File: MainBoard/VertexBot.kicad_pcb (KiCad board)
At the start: 2 copper layers, 115.6 x 107.8 mm, 47 parts, among them J1 Battery, J4 Left Motor, J5 Right Motor, J6 Led Strip, Q1 BSS138, Q2 BSS138, Q3 BSS138, SW1 SW_SPST, U1 DRV8830DGQR, U10 MAX4466, U11 MAX4466, U12 ESP32-S3-CAM-B, U13 ESP32-S3-CAM-A, U14 MAX98357A, U2 DRV8830DGQR, U3 S13V30F5, U5 INMP441, U6 0.96 INCH OLED, U7 DRV5033AJxLPG, U8 DRV5033AJxLPG, U9 MPU 6050

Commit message: Fix for correct battery connector footprint
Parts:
- J1: footprint Connector_JST:JST_XH_S3B-XH-A-1_1x03_P2.50mm_Horizontal -> Connector_JST:JST_XH_S2B-XH-A-1_1x02_P2.50mm_Horizontal
- moved J1 49.0 mm to (158.0, 113.6), turned to -125.5 degrees
- moved U5 16.5 mm to (107.3, 129.7)
- moved U9 4.93 mm to (147.2, 88.8)

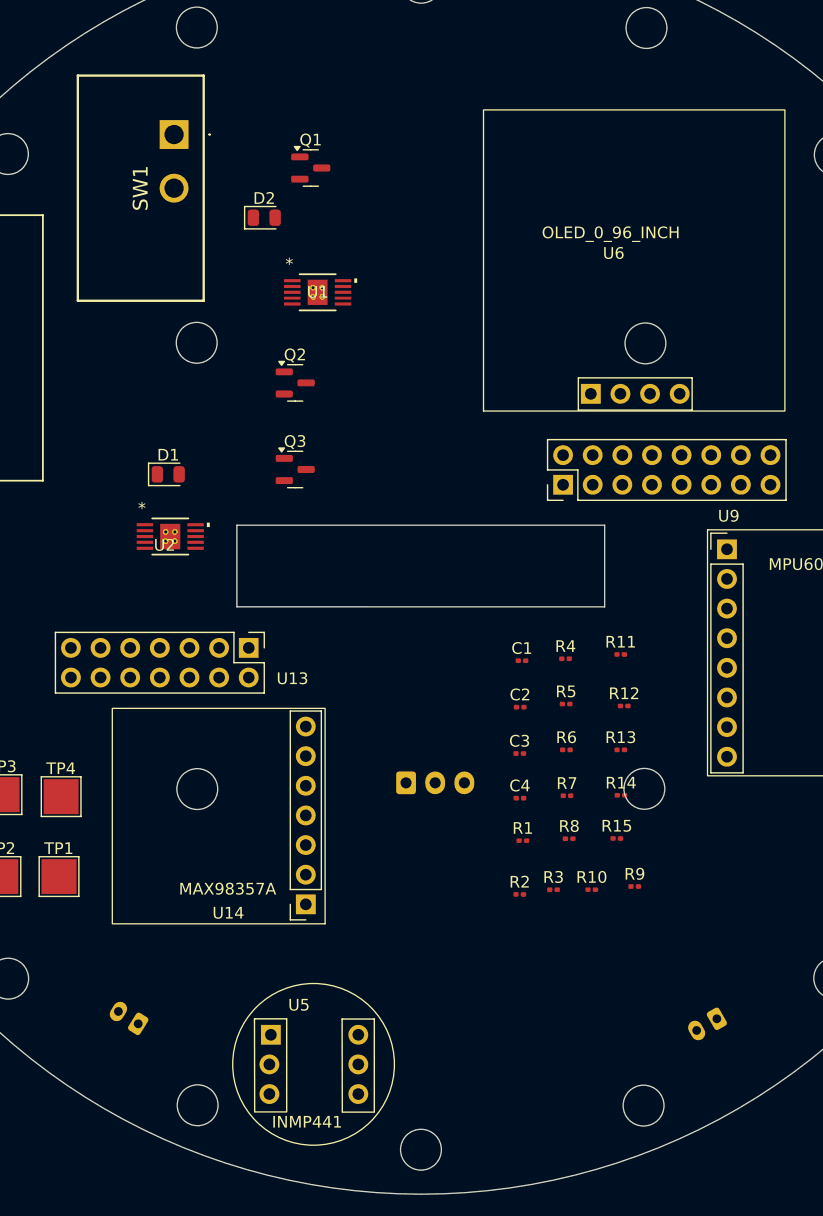
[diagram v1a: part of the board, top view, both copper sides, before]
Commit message: Adjust divider values for cutoff at 3V (en = 1V) Add Tolerance (0.1%)
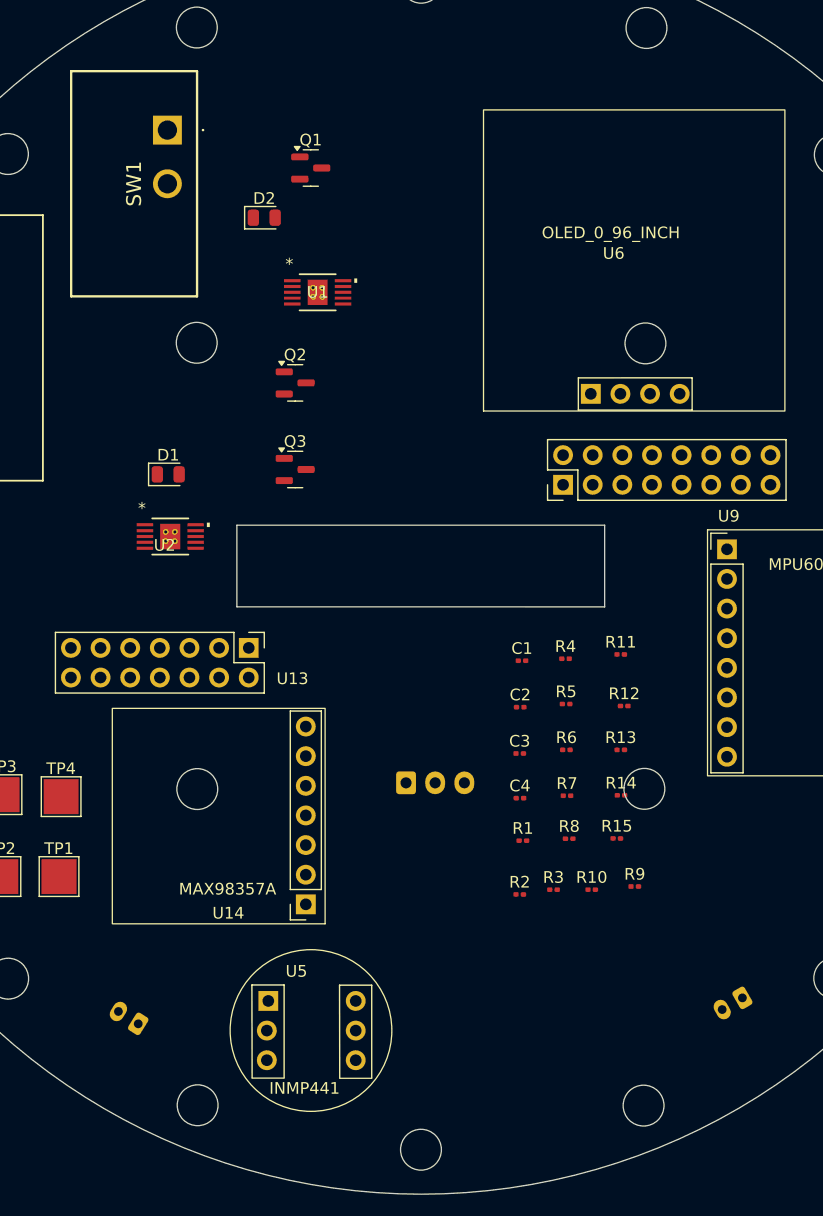
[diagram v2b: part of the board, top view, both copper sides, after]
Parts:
- moved U5 2.91 mm to (107.0, 126.8)
- moved J4 2.83 mm to (147.8, 126.5)
- moved SW1 0.69 mm to (98.5, 52.1)
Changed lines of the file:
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@@
 	(footprint "Vertex_Bot:L101011MS02Q"
 		(layer "F.Cu")
-		(at 99.09 52.52 -90)
+		(at 98.52 52.14 -90)
 		(descr "L101011MS02Q-2")
 		(tags "Switch")
@@
 	(footprint "Vertex_Bot:INMP441"
 		(layer "F.Cu")
-		(at 107.26 129.68)
+		(at 107.04 126.78)
 		(property "Reference" "U5"
 			(at 2.54 -2.54 0)
@@
 	(footprint "Connector_JST:JST_PH_S2B-PH-K_1x02_P2.00mm_Horizontal"
 		(layer "B.Cu")
-		(at 145.612051 128.31 -150)
+		(at 147.801026 126.518238 -150)
 		(descr "JST PH series connector, S2B-PH-K (http://www.jst-mfg.com/product/pdf/eng/ePH.pdf), generated with kicad-footprint-generator")
 		(tags "connector JST PH horizontal")
 		(property "Reference" "J4"
-			(at 1 2.55 30)
+			(at 0.999999 2.550002 30)
 			(layer "B.SilkS")
 			(effects
@@
 		)
 		(property "Value" "Left Motor"
-			(at 1 -7.45 30)
+			(at 1.000001 -7.449998 30)
 			(layer "B.Fab")
 			(effects
@@
 		(fp_line
 			(start 3.14 1.46)
-			(end 3.14 -0.14)
+			(end 3.14 -0.140002)
 			(stroke
 				(width 0.12)
@@
 		(fp_line
 			(start 4.06 -0.14)
-			(end 3.14 -0.14)
+			(end 3.14 -0.140002)
 			(stroke
 				(width 0.12)
@@
 		)
 		(fp_line
-			(start 3.14 -0.14)
+			(start 3.14 -0.140002)
 			(end 2.860001 -0.14)
 			(stroke
@@
 		(fp_line
 			(start 3.3 -2.5)
-			(end 3.3 -4.1)
+			(end 3.3 -4.100001)
 			(stroke
 				(width 0.12)
@@
 		)
 		(fp_line
-			(start 3.3 -4.1)
+			(start 3.3 -4.100001)
 			(end 2.3 -4.1)
 			(stroke
@@
 		)
 		(fp_line
-			(start 2.3 -2.500001)
+			(start 2.3 -2.500002)
 			(end 3.3 -2.5)
 			(stroke
@@
 		(fp_line
 			(start 2.3 -4.1)
-			(end 2.3 -2.500001)
+			(end 2.3 -2.500002)
 			(stroke
 				(width 0.12)
@@
 		(fp_line
 			(start -1.14 1.46)
-			(end -2.06 1.46)
+			(end -2.059999 1.460001)
 			(stroke
 				(width 0.12)
@@
 		)
 		(fp_line
-			(start -0.86 -0.14)
-			(end -0.86 1.075)
+			(start -0.860001 -0.140001)
+			(end -0.86 1.075001)
 			(stroke
 				(width 0.12)
@@
 		)
 		(fp_line
-			(start -0.86 -0.14)
+			(start -0.860001 -0.140001)
 			(end -1.14 -0.14)
 			(stroke
@@
 		)
 		(fp_line
-			(start -2.06 1.46)
-			(end -2.059999 -6.36)
+			(start -2.059999 1.460001)
+			(end -2.060002 -6.36)
 			(stroke
 				(width 0.12)
@@
 		(fp_line
 			(start -0.3 -2.500001)
-			(end -1.3 -2.5)
+			(end -1.299999 -2.5)
 			(stroke
 				(width 0.12)
@@
 		)
 		(fp_line
-			(start -2.059999 -0.14)
+			(start -2.06 -0.140001)
 			(end -1.14 -0.14)
 			(stroke
@@
 		)
 		(fp_line
-			(start -0.3 -4.1)
+			(start -0.299999 -4.1)
 			(end -0.3 -2.500001)
 			(stroke
@@
 		)
 		(fp_line
-			(start -0.3 -4.1)
-			(end -0.3 -6.360001)
+			(start -0.299999 -4.1)
+			(end -0.299998 -6.36)
 			(stroke
 				(width 0.12)
@@
 		)
 		(fp_line
-			(start -1.3 -2.5)
-			(end -1.3 -4.1)
+			(start -1.299999 -2.5)
+			(end -1.300001 -4.099999)
 			(stroke
 				(width 0.12)
@@
 		(fp_line
 			(start -0.8 -4.1)
-			(end -0.8 -6.36)
+			(end -0.799998 -6.360001)
 			(stroke
 				(width 0.12)
@@
 		)
 		(fp_line
-			(start 0.5 -6.36)
+			(start 0.500001 -6.36)
 			(end 0.5 -2)
 			(stroke
@@
 		)
 		(fp_line
-			(start -1.3 -4.1)
-			(end -0.3 -4.1)
+			(start -1.300001 -4.099999)
+			(end -0.299999 -4.1)
 			(stroke
 				(width 0.12)
@@
 		)
 		(fp_line
-			(start -2.059999 -6.36)
+			(start -2.060002 -6.36)
 			(end 4.06 -6.36)
 			(stroke
@@
 		(fp_line
 			(start -2.45 1.85)
-			(end -2.45 -6.749999)
+			(end -2.449999 -6.749999)
 			(stroke
 				(width 0.05)
@@
 		)
 		(fp_line
-			(start -2.45 -6.749999)
+			(start -2.449999 -6.749999)
 			(end 4.45 -6.75)
 			(stroke
@@
 		)
 		(fp_line
-			(start 3.95 1.35)
+			(start 3.949999 1.349998)
 			(end 3.250001 1.35)
 			(stroke
@@
 		)
 		(fp_line
-			(start 3.95 -6.25)
-			(end 3.95 1.35)
+			(start 3.95 -6.250003)
+			(end 3.949999 1.349998)
 			(stroke
 				(width 0.1)
@@
 		(fp_line
 			(start -1.25 1.35)
-			(end -1.95 1.35)
+			(end -1.95 1.350001)
 			(stroke
 				(width 0.1)
@@
 		)
 		(fp_line
-			(start -1.95 1.35)
-			(end -1.95 -6.25)
+			(start -1.95 1.350001)
+			(end -1.950001 -6.25)
 			(stroke
 				(width 0.1)
@@
 		)
 		(fp_line
-			(start -1.95 -6.25)
-			(end 3.95 -6.25)
+			(start -1.950001 -6.25)
+			(end 3.95 -6.250003)
 			(stroke
 				(width 0.1)

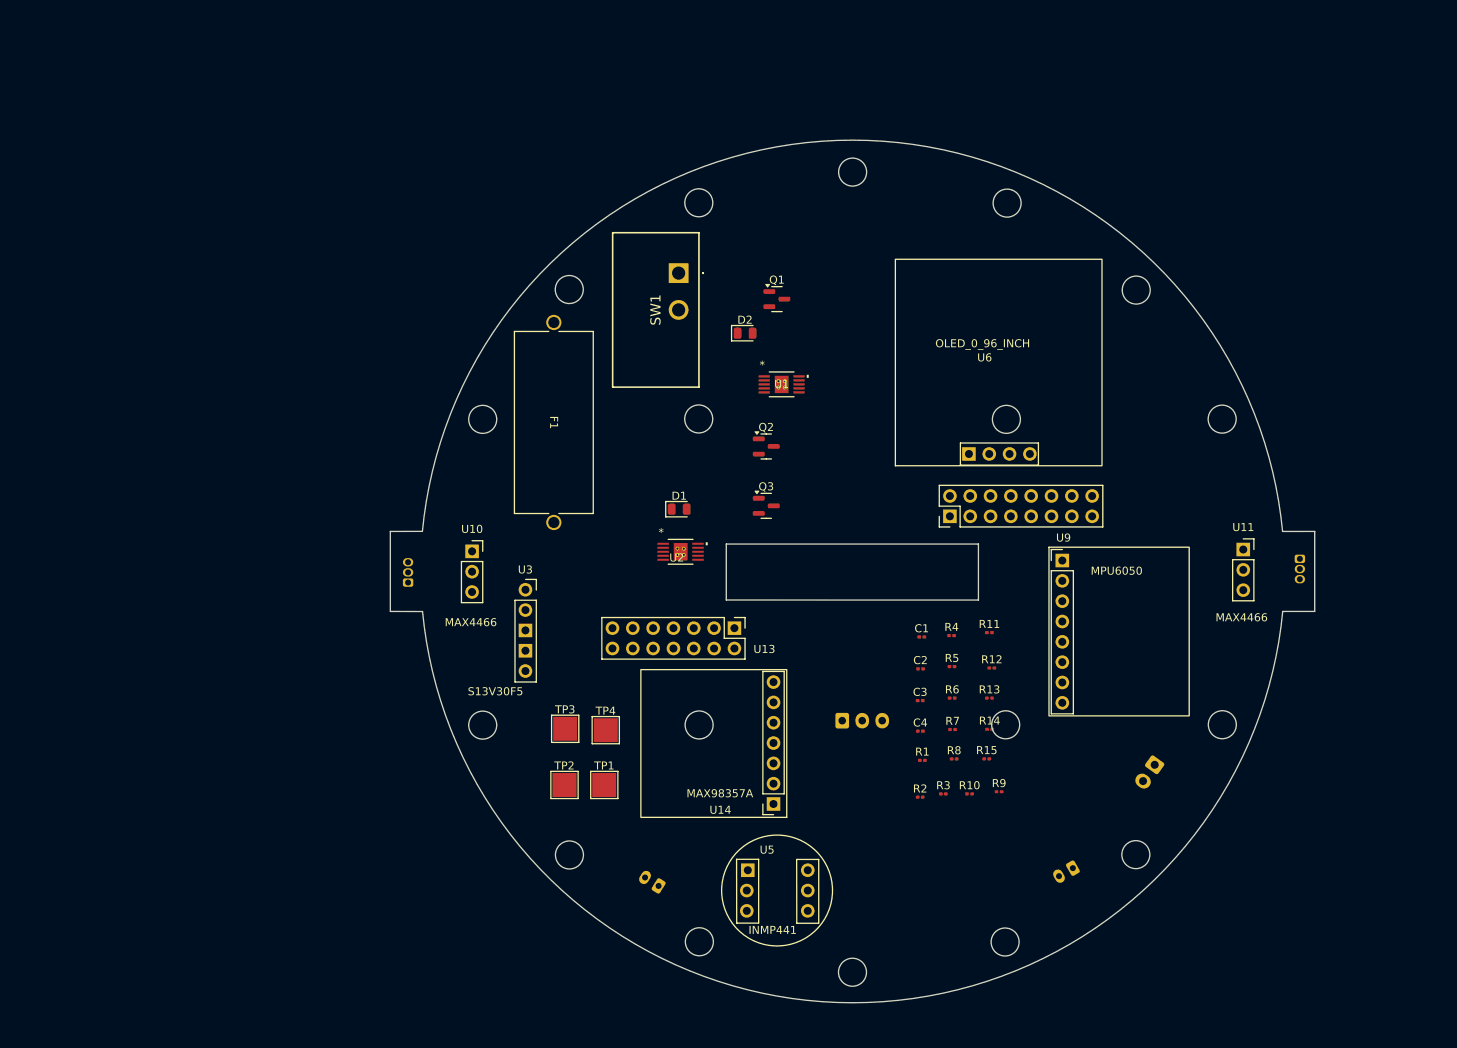
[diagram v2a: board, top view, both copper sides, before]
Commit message: - Relayed schematic with better modular approach (Global labels usage) - Edge cut so that now backboards are facing to the sides, central rectangular hole rotated by 90 - Some fooprints DRC'ed and fixed (more to come)
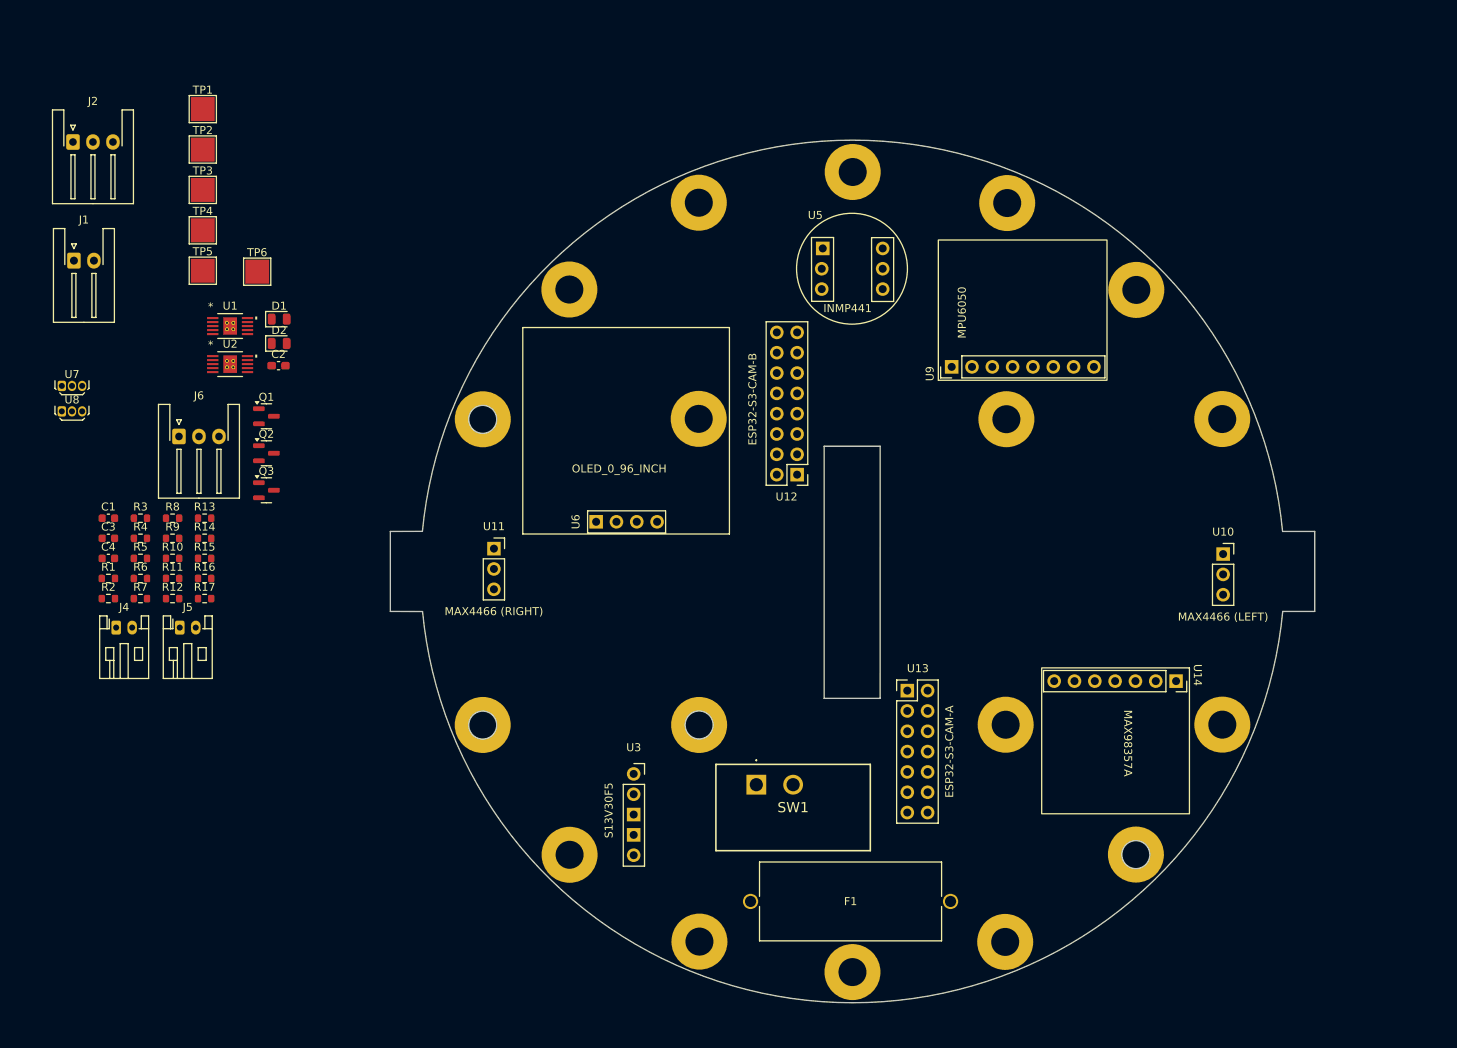
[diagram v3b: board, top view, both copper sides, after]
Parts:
- added H1: MountingHole, MountingHole:MountingHole_3.5mm_Pad, F.Cu at (139.5, 70.4)
- added H10: MountingHole, MountingHole:MountingHole_3.5mm_Pad, F.Cu at (155.7, 124.8)
- added H11: MountingHole, MountingHole:MountingHole_3.5mm_Pad, F.Cu at (139.3, 135.7)
- added H12: MountingHole, MountingHole:MountingHole_3.5mm_Pad, F.Cu at (120.2, 139.5)
- added H13: MountingHole, MountingHole:MountingHole_3.5mm_Pad, F.Cu at (101.1, 135.7)
- added H14: MountingHole, MountingHole:MountingHole_3.5mm_Pad, F.Cu at (84.9, 124.8)
- added H15: MountingHole, MountingHole:MountingHole_3.5mm_Pad, F.Cu at (74.0, 108.6)
- added H16: MountingHole, MountingHole:MountingHole_3.5mm_Pad, F.Cu at (74.0, 70.4)
- added H17: MountingHole, MountingHole:MountingHole_3.5mm_Pad, F.Cu at (84.9, 54.2)
- added H18: MountingHole, MountingHole:MountingHole_3.5mm_Pad, F.Cu at (101.0, 43.3)
- added H2: MountingHole, MountingHole:MountingHole_3.5mm_Pad, F.Cu at (101.0, 70.4)
- added H3: MountingHole, MountingHole:MountingHole_3.5mm_Pad, F.Cu at (101.1, 108.6)
- added H4: MountingHole, MountingHole:MountingHole_3.5mm_Pad, F.Cu at (139.4, 108.6)
- added H5: MountingHole, MountingHole:MountingHole_3.5mm_Pad, F.Cu at (120.3, 39.5)
- added H6: MountingHole, MountingHole:MountingHole_3.5mm_Pad, F.Cu at (139.6, 43.4)
- added H7: MountingHole, MountingHole:MountingHole_3.5mm_Pad, F.Cu at (155.7, 54.2)
- added H8: MountingHole, MountingHole:MountingHole_3.5mm_Pad, F.Cu at (166.5, 70.4)
- added H9: MountingHole, MountingHole:MountingHole_3.5mm_Pad, F.Cu at (166.5, 108.6)
- added J2: I2C Extension, Connector_JST:JST_XH_S3B-XH-A-1_1x03_P2.50mm_Horizontal, F.Cu at (22.8, 35.8)
- added R16: 0.44, Resistor_SMD:R_0603_1608Metric, F.Cu at (39.3, 90.3)
- added R17: 0.44, Resistor_SMD:R_0603_1608Metric, F.Cu at (39.3, 92.8)
- added TP5: TestPoint_Flag, TestPoint:TestPoint_Pad_3.0x3.0mm, F.Cu at (39.0, 51.8)
- added TP6: TestPoint_Flag, TestPoint:TestPoint_Pad_3.0x3.0mm, F.Cu at (45.8, 52.0)
- C1: footprint Capacitor_SMD:C_0201_0603Metric -> Capacitor_SMD:C_0603_1608Metric
- C2: footprint Capacitor_SMD:C_0201_0603Metric -> Capacitor_SMD:C_0603_1608Metric_Pad1.08x0.95mm_HandSolder
- C3, C4: value 10uF -> 100nF; footprint Capacitor_SMD:C_0201_0603Metric -> Capacitor_SMD:C_0603_1608Metric
- J1, J4, J5, J6, U7, U8: moved to F.Cu
- R1: value 10K -> 20K 0.1%; footprint Resistor_SMD:R_0201_0603Metric -> Resistor_SMD:R_0603_1608Metric
- R10, R11, R12, R14, R15, R2, R3, R4, R5, R6, R7: footprint Resistor_SMD:R_0201_0603Metric -> Resistor_SMD:R_0603_1608Metric
- R13: value 15K -> 10K 0.1%; footprint Resistor_SMD:R_0201_0603Metric -> Resistor_SMD:R_0603_1608Metric
- R8, R9: value 0.22 -> 0.44; footprint Resistor_SMD:R_0201_0603Metric -> Resistor_SMD:R_0603_1608Metric
- U10: value MAX4466 -> MAX4466 (LEFT)
- U11: value MAX4466 -> MAX4466 (RIGHT)
- moved U8 155.8 mm to (21.4, 69.4), turned to 0 degrees
- moved J1 149.1 mm to (22.9, 50.6), turned to 0 degrees
- moved J4 123.3 mm to (28.2, 96.5), turned to 0 degrees
- moved R9 108.1 mm to (35.3, 85.3)
- moved R3 106.1 mm to (31.2, 82.8)
- moved R2 104.5 mm to (27.2, 92.8)
- moved R1 104.3 mm to (27.2, 90.3)
- moved R10 103.9 mm to (35.3, 87.8)
- moved C4 103.8 mm to (27.2, 87.8)
- moved C3 103.5 mm to (27.2, 85.3)
- moved R7 102.8 mm to (31.2, 92.8)
- moved R12 102.8 mm to (35.3, 92.8)
- moved C1 102.7 mm to (27.2, 82.8)
- moved R6 102.6 mm to (31.2, 90.3)
- moved R5 102.3 mm to (31.2, 87.8)
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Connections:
- net Net-(J6-Pin_2) renamed WLED-5V
- net Net-(Q1-D) renamed SCL
- net Net-(Q1-S) renamed SCL-3.3
- net Net-(Q2-D) renamed SDA
- net Net-(Q2-S) renamed SDA-3.3
- net Net-(Q3-S) renamed WLED-3.3V
- net Net-(U10-OUT) renamed MIC_A
- net Net-(U11-OUT) renamed MIC_B
- net Net-(U12-AMP_BCLK) renamed AMP_BCLK
- net Net-(U12-AMP_LRCLK) renamed AMP_LRCLK
- net Net-(U12-APM_DOUT) renamed AMP_DOUT
- net Net-(U12-MIC_BCLK) renamed MIC_BCLK
- net Net-(U12-MIC_DIN) renamed MIC_DIN
- net Net-(U12-MIC_LRCLK) renamed MIC_LRCLK
- net Net-(U12-SYNC_FOLLOW) renamed SYNC
- net Net-(U12-UART_RX) renamed TX
- net Net-(U12-UART_TX) renamed RX
- net Net-(U13-IMU_INTR) renamed INT
- net Net-(U13-LEFT_WHEEL) renamed LEFT_WHEEL
- net Net-(U13-RIGHT_WHEEL) renamed RIGHT_WHEEL
- C1 pad 1: Net-(Q1-G) -> 3.3V-A
- C2 pad 1: Net-(Q1-G) -> 3.3V-A
- C3 pad 1: +5V -> 5V
- C4 pad 1: +5V -> 5V
- J1 pad 2: GND -> Net-(J1-Pin_2)
- J6 pad 1: +5V -> 5V
- Q1 pad 1: Net-(Q1-G) -> 3.3V-A
- Q2 pad 1: Net-(Q1-G) -> 3.3V-A
- Q3 pad 1: Net-(Q1-G) -> 3.3V-A
- R10 pad 1: Net-(U14-GAIN) -> GND
- R10 pad 2: GND -> Net-(U14-GAIN)
- R11 pad 1: Net-(Q1-G) -> 3.3V-A
- R12 pad 1: Net-(Q1-G) -> 3.3V-A
- R14 pad 1: Net-(D1-A) -> 5V
- R14 pad 2: +5V -> Net-(D1-A)
- R15 pad 1: Net-(D2-A) -> 5V
- R15 pad 2: +5V -> Net-(D2-A)
- R2 pad 2: Net-(Q1-G) -> 3.3V-A
- R3 pad 1: +5V -> 5V
- R4 pad 1: +5V -> 5V
- R5 pad 1: +5V -> 5V
- R6 pad 2: Net-(Q1-G) -> 3.3V-A
- R7 pad 2: Net-(Q1-G) -> 3.3V-A
- R8 pad 1: Net-(U2-ISENSE) -> GND
- R8 pad 2: GND -> Net-(U2-ISENSE)
- SW1 pad 1: GND -> Net-(J1-Pin_2)
- TP1 pad 1: GND -> Net-(J1-Pin_2)
- TP2 pad 1: Net-(Q1-G) -> 3.3V-A
- U1 pad 4: +5V -> 5V
- U1 pad EPAD: (no net) -> GND
- U10 pad 3: Net-(Q1-G) -> 3.3V-A
- U11 pad 3: Net-(Q1-G) -> 3.3V-B
- U12 pad 1: +5V -> 5V
- U12 pad 14: Net-(U12-3.3V) -> 3.3V-B
- U13 pad 1: +5V -> 5V
- U13 pad 14: Net-(Q1-G) -> 3.3V-A
- U14 pad 5: Net-(U12-3.3V) -> 3.3V-B
- U14 pad 7: +5V -> 5V
- U2 pad 4: +5V -> 5V
- U2 pad EPAD: (no net) -> GND
- U3 pad 5: +5V -> 5V
- U5 pad 1: Net-(U12-3.3V) -> 3.3V-B
- U5 pad 5: Net-(U12-3.3V) -> 3.3V-B
- U6 pad 3: +5V -> 5V
- U7 pad 1: Net-(Q1-G) -> 3.3V-A
- U8 pad 1: Net-(Q1-G) -> 3.3V-A
- U9 pad 1: Net-(Q1-G) -> 3.3V-A
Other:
- outline, holes or cut-outs redrawn
- board text added: "U11"
